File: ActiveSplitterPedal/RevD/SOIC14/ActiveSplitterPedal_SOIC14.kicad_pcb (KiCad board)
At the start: 2 copper layers, 112.5 x 86.4 mm, 81 parts, among them J1 MonoJack2Switch, J2 Barrel_Jack, J3 MonoJack2Switch, J4 MonoJack2Switch, J5 MonoJack2Switch, J6 MonoJack2Switch, U1 SE8250X2, U11 TL072, U12 TL074, U14 ISA0505, U15 MCP1754S-3302xCB, U16 TC593002ECB, U2 TL072, U3 TL074, U5 TL072, U6 TL074, U8 TL072, U9 TL074

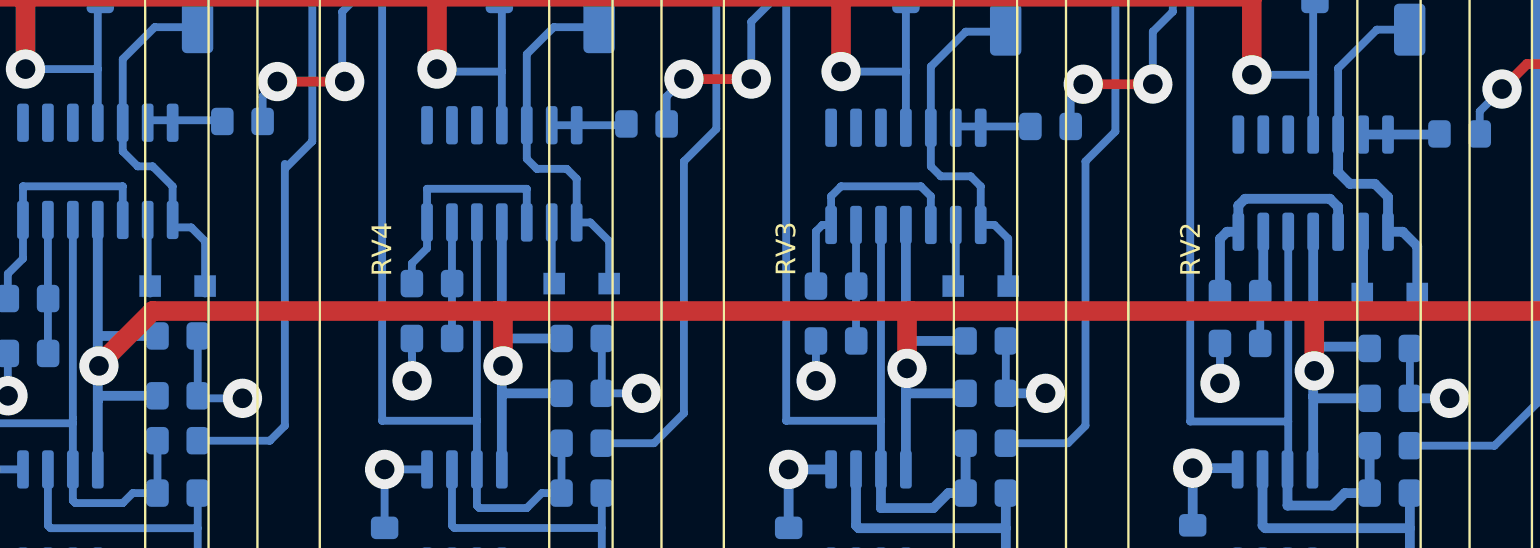
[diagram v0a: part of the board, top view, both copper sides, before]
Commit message: fixed peak detector
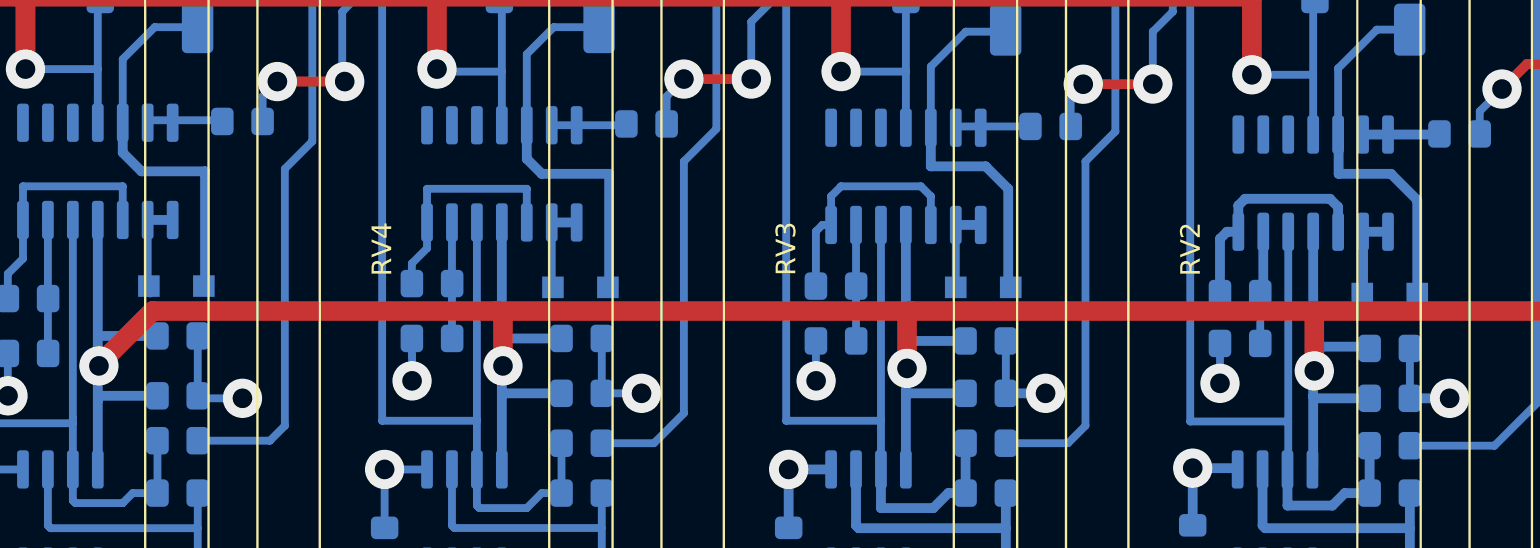
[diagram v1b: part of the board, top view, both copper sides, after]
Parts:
- C14, C25, C36, C47: value 1pF -> 1nF
- D1, D3, D5, D7: value D_Schottky -> 1N914
- U1: value SE8250X2 -> AP7370-50SA-7
- moved D5 0.20 mm to (122.9, 100.6)
- moved D3 0.14 mm to (143.4, 100.6)
- moved D7 0.06 mm to (102.3, 100.6)
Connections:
- U12 pad 1: Net-(C39-Pad1) -> Net-(D7-Pad2)
- U3 pad 1: Net-(C6-Pad1) -> Net-(D1-Pad2)
- U6 pad 1: Net-(C17-Pad1) -> Net-(D3-Pad2)
- U9 pad 1: Net-(C28-Pad1) -> Net-(D5-Pad2)
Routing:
- net Net-(D3-Pad2): track 3.17 -> 4.44 mm
- net Net-(D7-Pad2): track 3.42 -> 4.69 mm
- net Net-(D1-Pad2): track 3.16 -> 4.43 mm
- net Net-(D5-Pad2): track 3.16 -> 4.43 mm
- net Net-(C28-Pad1): track 19.0 -> 19.7 mm
- net Net-(C39-Pad1): track 19.7 -> 20.2 mm

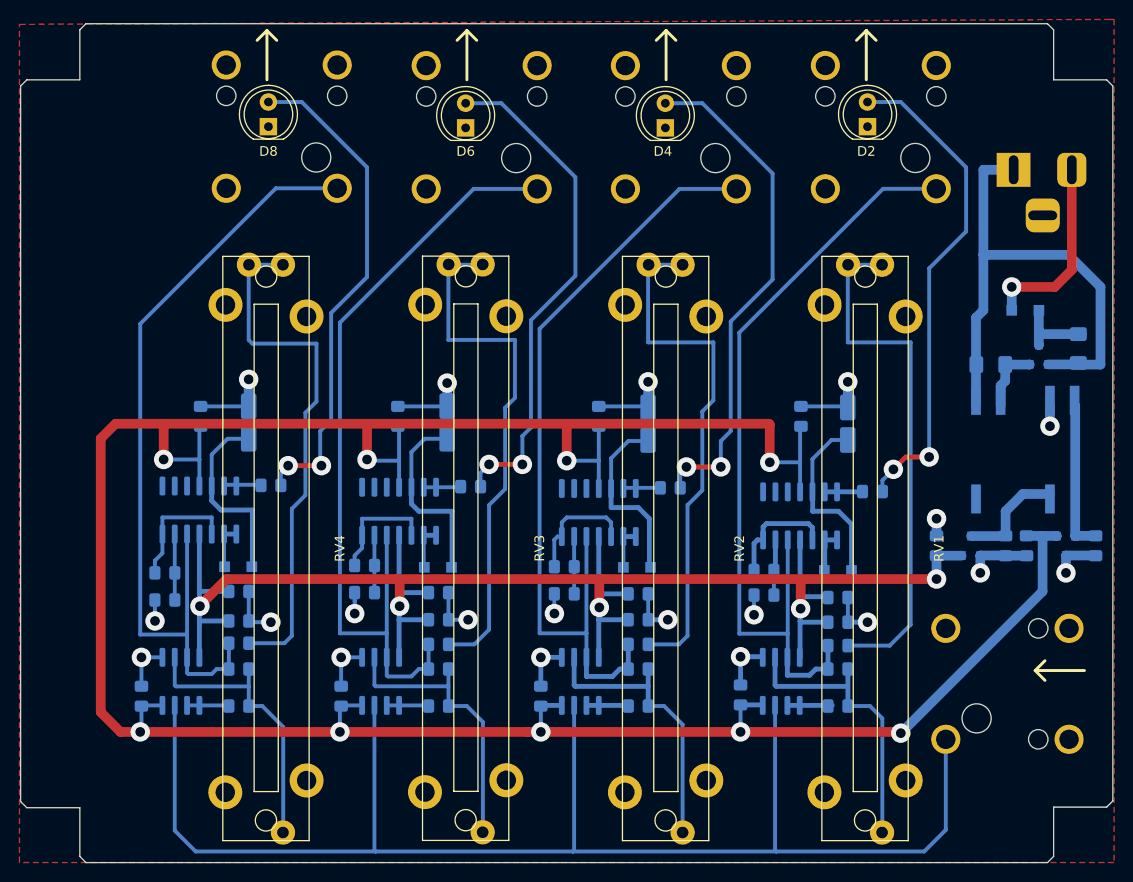
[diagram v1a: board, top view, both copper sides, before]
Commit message: updated layout
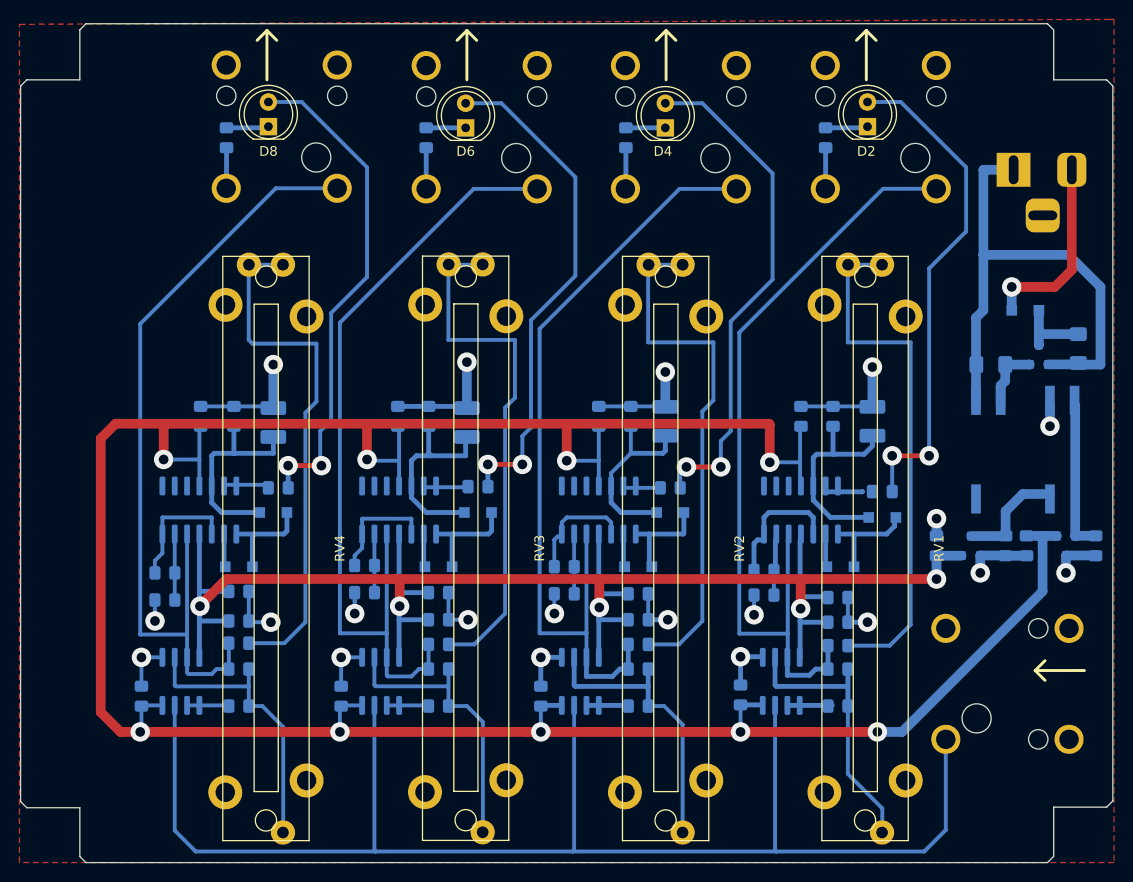
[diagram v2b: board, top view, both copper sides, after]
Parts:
- added D10: 1N914, Diode_SMD:D_SOD-123F, B.Cu at (164.3, 100.6)
- added D11: 1N914, Diode_SMD:D_SOD-123F, B.Cu at (143.5, 100.6)
- added D12: 1N914, Diode_SMD:D_SOD-123F, B.Cu at (122.9, 100.6)
- added D13: 1N914, Diode_SMD:D_SOD-123F, B.Cu at (102.4, 100.6)
- added R10: 10M 1%, Resistor_SMD:R_0805_2012Metric_Pad1.15x1.40mm_HandSolder, B.Cu at (142.7, 85.1)
- added R16: 10M 1%, Resistor_SMD:R_0805_2012Metric_Pad1.15x1.40mm_HandSolder, B.Cu at (121.9, 85.1)
- added R22: 10M 1%, Resistor_SMD:R_0805_2012Metric_Pad1.15x1.40mm_HandSolder, B.Cu at (101.9, 85.1)
- added R25: 100R, Capacitor_SMD:C_0805_2012Metric_Pad1.15x1.40mm_HandSolder, B.Cu at (162.8, 56.4)
- added R26: 100R, Capacitor_SMD:C_0805_2012Metric_Pad1.15x1.40mm_HandSolder, B.Cu at (142.2, 56.4)
- added R27: 100R, Capacitor_SMD:C_0805_2012Metric_Pad1.15x1.40mm_HandSolder, B.Cu at (121.7, 56.4)
- added R28: 100R, Capacitor_SMD:C_0805_2012Metric_Pad1.15x1.40mm_HandSolder, B.Cu at (101.1, 56.4)
- added R4: 10M 1%, Resistor_SMD:R_0805_2012Metric_Pad1.15x1.40mm_HandSolder, B.Cu at (163.6, 85.1)
- C17, C28, C39, C6: value 1uF -> 470uF 1%; footprint Capacitor_SMD:C_Elec_4x5.8 -> Capacitor_SMD:C_1210_3225Metric_Pad1.42x2.65mm_HandSolder
- moved D1 7.12 mm to (168.7, 95.5), turned to 0 degrees
- moved D5 7.00 mm to (127.0, 95.0), turned to 0 degrees
- moved D7 6.66 mm to (105.9, 95.0), turned to 0 degrees
- moved D3 6.61 mm to (146.8, 95.0), turned to 0 degrees
- moved C6 2.55 mm to (167.6, 85.6)
- moved C39 2.54 mm to (105.9, 85.7)
- moved C28 2.03 mm to (125.9, 85.7)
- moved C17 1.80 mm to (146.3, 85.6)
- moved R3 1.02 mm to (168.7, 92.8)
- moved R21 0.80 mm to (106.4, 92.5)
- moved R15 0.76 mm to (127.0, 92.3)
- moved U3 0.61 mm to (160.3, 94.7)
- moved U6 0.25 mm to (139.4, 94.7)
- moved U9 0.13 mm to (118.9, 94.7)
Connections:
- D3 pad 2: Net-(D3-Pad2) -> Net-(D11-Pad1)
- D5 pad 2: Net-(D5-Pad2) -> Net-(D12-Pad1)
- D7 pad 2: Net-(D7-Pad2) -> Net-(D13-Pad1)
- J3 pad 2: VCOM -> Net-(J3-Pad2)
- J4 pad 2: VCOM -> Net-(J4-Pad2)
- J5 pad 2: VCOM -> Net-(J5-Pad2)
- J6 pad 2: VCOM -> Net-(J6-Pad2)
- U12 pad 1: Net-(D7-Pad2) -> Net-(D13-Pad1)
- U12 pad 2: Net-(D7-Pad2) -> Net-(D13-Pad2)
- U3 pad 2: Net-(D1-Pad2) -> Net-(D10-Pad2)
- U6 pad 1: Net-(D3-Pad2) -> Net-(D11-Pad1)
- U6 pad 2: Net-(D3-Pad2) -> Net-(D11-Pad2)
- U9 pad 1: Net-(D5-Pad2) -> Net-(D12-Pad1)
- U9 pad 2: Net-(D5-Pad2) -> Net-(D12-Pad2)
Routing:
- net VCOM: track 93.4 -> 124.9 mm
- net Net-(D12-Pad1): track 0.00 -> 11.1 mm
- net Net-(D13-Pad1): track 0.00 -> 10.7 mm
- net Net-(D11-Pad1): track 0.00 -> 10.0 mm
- net Net-(D1-Pad2): track 4.43 -> 10.5 mm
- net Net-(D7-Pad2): track 4.69 -> 0.00 mm
- net Net-(D3-Pad2): track 4.44 -> 0.00 mm
- net Net-(D5-Pad2): track 4.43 -> 0.00 mm
- net Net-(J4-Pad2): track 0.00 -> 4.27 mm
- net Net-(J5-Pad2): track 0.00 -> 4.25 mm
- net Net-(J3-Pad2): track 0.00 -> 4.24 mm
- net Net-(J6-Pad2): track 0.00 -> 4.19 mm
- net Net-(D11-Pad2): track 0.00 -> 3.42 mm
- net Net-(D13-Pad2): track 0.00 -> 3.42 mm
- net Net-(D12-Pad2): track 0.00 -> 3.42 mm
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
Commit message: Completed RevD
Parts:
- added REF**: 1590BB, Hammond1590:1590BB, F.Cu at (136.1, 87.9)
- added TP1: TestPoint, TestPoint:TestPoint_Pad_1.0x1.0mm, B.Cu at (174.2, 104.5)
- added TP2: TestPoint, TestPoint:TestPoint_Pad_1.0x1.0mm, B.Cu at (181.4, 104.5)
- added TP3: TestPoint, TestPoint:TestPoint_Pad_1.0x1.0mm, B.Cu at (187.6, 104.5)
- R25, R26, R27, R28: moved to F.Cu
- moved R28 11.8 mm to (95.6, 66.8), turned to 270 degrees
- moved R25 11.6 mm to (157.7, 66.8), turned to 270 degrees
- moved R26 11.5 mm to (137.4, 66.8), turned to 270 degrees
- moved R27 11.4 mm to (117.1, 66.8), turned to 270 degrees
- moved J1 2.67 mm to (181.4, 115.3)
- moved D1 0.64 mm to (168.7, 94.9)
- moved R3 0.64 mm to (168.7, 92.2)
- moved D2 0.13 mm to (167.0, 55.2)
- moved D4 0.13 mm to (146.4, 55.4)
- moved RV1 0.13 mm to (167.0, 98.7)
- moved D6 0.13 mm to (125.9, 55.4)
- moved D8 0.13 mm to (105.3, 55.2)
- moved RV3 0.13 mm to (125.8, 98.8)
- moved RV2 0.10 mm to (146.4, 98.7)
- moved RV4 0.10 mm to (105.3, 98.7)
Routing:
- net VCOM: track 124.9 -> 115.6 mm
- net Net-(J3-Pad2): track 4.24 -> 8.14 mm
- net Net-(J6-Pad2): track 4.19 -> 8.06 mm
- net Net-(J5-Pad2): track 4.25 -> 7.61 mm
- net Net-(J4-Pad2): track 4.27 -> 7.51 mm
- net -3V3: track 285.7 -> 288.8 mm
- net +3V3: track 164.5 -> 167.5 mm
- net /InputBuffer1/SIGNAL_INPUT: track 148.8 -> 146.1 mm
- net Net-(R3-Pad2): track 3.90 -> 4.84 mm
- net Net-(D1-Pad2): track 10.5 -> 11.2 mm
- net Net-(D2-Pad2): track 51.7 -> 51.2 mm
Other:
- board text added: "+3V"
- board text added: "-3V"
- board text added: "9VDC 150mA Center Negative!"
- board text added: "Active 4-Way Splitter RevD 3720"
- board text removed: "Active 4-Way Splitter RevA"

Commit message: updated hw
- Changed peak detector gain feedback resistor to 10K
- Changed peak detector storage cap to 100nF
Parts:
- C17, C28, C39, C6: value 470uF 1% -> 100nF 1%
- R14, R2, R20, R8: value 120K -> 10K
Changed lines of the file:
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@@
       (effects (font (size 1 1) (thickness 0.15)) (justify mirror))
     )
-    (fp_text value "470uF 1%" (at 0 -2.28 90) (layer B.Fab)
+    (fp_text value "100nF 1%" (at 0 -2.28 90) (layer B.Fab)
       (effects (font (size 1 1) (thickness 0.15)) (justify mirror))
     )
@@
       (effects (font (size 1 1) (thickness 0.15)) (justify mirror))
     )
-    (fp_text value "470uF 1%" (at 0 -2.28 90) (layer B.Fab)
+    (fp_text value "100nF 1%" (at 0 -2.28 90) (layer B.Fab)
       (effects (font (size 1 1) (thickness 0.15)) (justify mirror))
     )
@@
       (effects (font (size 1 1) (thickness 0.15)) (justify mirror))
     )
-    (fp_text value "470uF 1%" (at 0 -2.28 90) (layer B.Fab)
+    (fp_text value "100nF 1%" (at 0 -2.28 90) (layer B.Fab)
       (effects (font (size 1 1) (thickness 0.15)) (justify mirror))
     )
@@
       (effects (font (size 1 1) (thickness 0.15)) (justify mirror))
     )
-    (fp_text value "470uF 1%" (at 0 -2.28 90) (layer B.Fab)
+    (fp_text value "100nF 1%" (at 0 -2.28 90) (layer B.Fab)
       (effects (font (size 1 1) (thickness 0.15)) (justify mirror))
     )
@@
       (effects (font (size 1 1) (thickness 0.15)) (justify mirror))
     )
-    (fp_text value 120K (at 0 -1.65) (layer B.Fab)
+    (fp_text value 10K (at 0 -1.65) (layer B.Fab)
       (effects (font (size 1 1) (thickness 0.15)) (justify mirror))
     )
@@
       (effects (font (size 1 1) (thickness 0.15)) (justify mirror))
     )
-    (fp_text value 120K (at 0 -1.65) (layer B.Fab)
+    (fp_text value 10K (at 0 -1.65) (layer B.Fab)
       (effects (font (size 1 1) (thickness 0.15)) (justify mirror))
     )
@@
       (effects (font (size 1 1) (thickness 0.15)) (justify mirror))
     )
-    (fp_text value 120K (at 0 -1.65) (layer B.Fab)
+    (fp_text value 10K (at 0 -1.65) (layer B.Fab)
       (effects (font (size 1 1) (thickness 0.15)) (justify mirror))
     )
@@
       (effects (font (size 1 1) (thickness 0.15)) (justify mirror))
     )
-    (fp_text value 120K (at 0 -1.65) (layer B.Fab)
-      (effects (font (size 1 1) (thickness 0.15)) (justify mirror))
-    )
+    (fp_text value 10K (at 0 -1.65) (layer B.Fab)
+      (effects (font (size 1 1) (thickness 0.15)) (justify mirror))
+    )
